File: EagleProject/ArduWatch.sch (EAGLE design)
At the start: 23 parts, among them IC1 DS1307Z, IC2 MCP73831, Q1 32.768Hz, U1 ATMEGA328P_TQFP

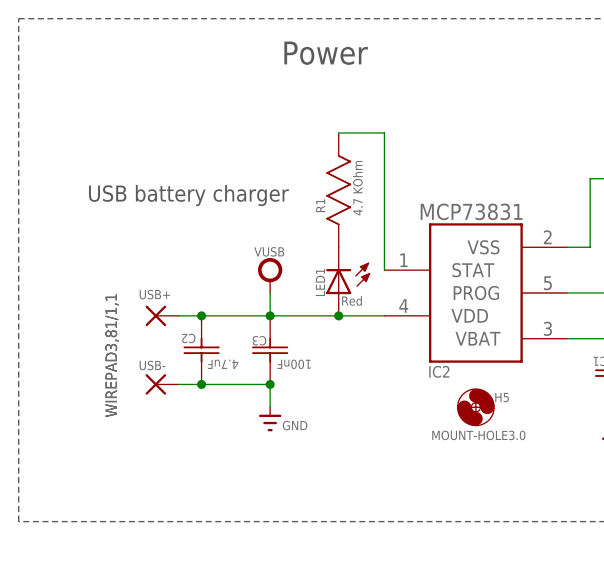
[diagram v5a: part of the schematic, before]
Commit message: USB port for charging
Implement USB port for chrging
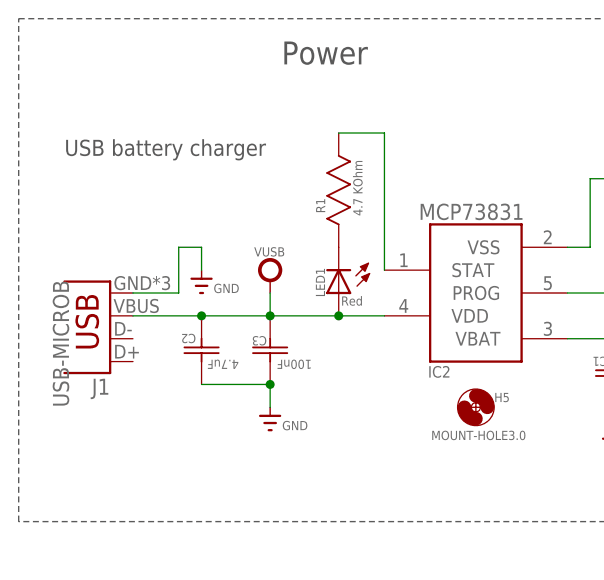
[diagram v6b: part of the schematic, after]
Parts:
- removed USB+, USB-: WIREPAD3,81/1,1, wirepad:WIREPAD3,81/1,1
- added J1: USB-MICROB, SparkFun-Connectors:USB-MICROB
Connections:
- net GND: now also J1.GND; no longer USB-.P
- net VUSB: now also J1.VBUS; no longer USB+.P
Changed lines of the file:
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@@
 <part name="Q1" library="crystal" deviceset="CRYSTAL" device="TC26H" value="32.768Hz"/>
 <part name="IC2" library="microchip-update" deviceset="MCP73831" device=""/>
-<part name="USB+" library="wirepad" deviceset="WIREPAD" device="3,81/1,1" value="WIREPAD3,81/1,1"/>
-<part name="USB-" library="wirepad" deviceset="WIREPAD" device="3,81/1,1" value="WIREPAD3,81/1,1"/>
 <part name="GND1" library="supply" deviceset="GND" device=""/>
 <part name="V1" library="supply" deviceset="VUSB" device=""/>
@@
 <part name="V8" library="supply" deviceset="VCC" device=""/>
 <part name="JP1" library="pinhead" deviceset="PINHD-2X3" device=""/>
+<part name="J1" library="SparkFun-Connectors" deviceset="USB" device="-MICROB"/>
+<part name="GND6" library="supply" deviceset="GND" device=""/>
 </parts>
 <sheets>
 <sheet>
 <plain>
-<text x="12.7" y="154.94" size="1.778" layer="97">USB battery charger</text>
+<text x="10.16" y="160.02" size="1.778" layer="97">USB battery charger</text>
 <wire x1="5.08" y1="175.26" x2="99.06" y2="175.26" width="0.1524" layer="97" style="longdash"/>
 <wire x1="99.06" y1="175.26" x2="99.06" y2="119.38" width="0.1524" layer="97" style="longdash"/>
@@
 <attribute name="VALUE" x="49.53" y="154.686" size="1.778" layer="96" rot="MR180"/>
 </instance>
-<instance part="USB+" gate="G$1" x="20.32" y="142.24" smashed="yes">
-<attribute name="NAME" x="18.415" y="144.0942" size="1.016" layer="95"/>
-<attribute name="VALUE" x="16.002" y="130.937" size="1.27" layer="96" rot="R90"/>
-</instance>
-<instance part="USB-" gate="G$1" x="20.32" y="134.62" smashed="yes">
-<attribute name="NAME" x="18.415" y="136.2202" size="1.016" layer="95"/>
-<attribute name="VALUE" x="16.002" y="130.937" size="1.27" layer="96" rot="R90"/>
-</instance>
 <instance part="GND1" gate="1" x="33.02" y="129.54" smashed="yes">
 <attribute name="VALUE" x="34.3535" y="129.54" size="1.016" layer="96"/>
@@
 </instance>
 <instance part="JP1" gate="A" x="218.44" y="43.18"/>
+<instance part="J1" gate="G$1" x="15.24" y="144.78" smashed="yes" rot="R180">
+<attribute name="NAME" x="15.24" y="135.255" size="1.778" layer="95" rot="R180"/>
+<attribute name="VALUE" x="8.89" y="132.08" size="1.778" layer="96" rot="MR90"/>
+</instance>
+<instance part="GND6" gate="1" x="25.4" y="144.78" smashed="yes">
+<attribute name="VALUE" x="26.7335" y="144.78" size="1.016" layer="96"/>
+</instance>
 </instances>
 <busses>
@@
 <net name="VUSB" class="0">
 <segment>
-<pinref part="USB+" gate="G$1" pin="P"/>
 <pinref part="LED1" gate="G$1" pin="A"/>
-<wire x1="22.86" y1="142.24" x2="25.4" y2="142.24" width="0.1524" layer="91"/>
 <pinref part="IC2" gate="G$1" pin="VDD"/>
 <wire x1="25.4" y1="142.24" x2="33.02" y2="142.24" width="0.1524" layer="91"/>
@@
 <junction x="25.4" y="142.24"/>
 <pinref part="C3" gate="A" pin="C2"/>
+<pinref part="J1" gate="G$1" pin="VBUS"/>
+<wire x1="25.4" y1="142.24" x2="17.78" y2="142.24" width="0.1524" layer="91"/>
 </segment>
 </net>
@@
 <pinref part="GND1" gate="1" pin="GND"/>
 <wire x1="33.02" y1="132.08" x2="33.02" y2="134.62" width="0.1524" layer="91"/>
-<pinref part="USB-" gate="G$1" pin="P"/>
 <wire x1="33.02" y1="134.62" x2="25.4" y2="134.62" width="0.1524" layer="91"/>
 <pinref part="C2" gate="A" pin="C1"/>
-<wire x1="25.4" y1="134.62" x2="22.86" y2="134.62" width="0.1524" layer="91"/>
-<junction x="25.4" y="134.62"/>
 <pinref part="C3" gate="A" pin="C1"/>
 <junction x="33.02" y="134.62"/>
@@
 <label x="231.14" y="40.64" size="1.016" layer="95" xref="yes"/>
 </segment>
+<segment>
+<pinref part="J1" gate="G$1" pin="GND"/>
+<wire x1="17.78" y1="144.78" x2="22.86" y2="144.78" width="0.1524" layer="91"/>
+<wire x1="22.86" y1="144.78" x2="22.86" y2="149.86" width="0.1524" layer="91"/>
+<pinref part="GND6" gate="1" pin="GND"/>
+<wire x1="22.86" y1="149.86" x2="25.4" y2="149.86" width="0.1524" layer="91"/>
+<wire x1="25.4" y1="149.86" x2="25.4" y2="147.32" width="0.1524" layer="91"/>
+</segment>
 </net>

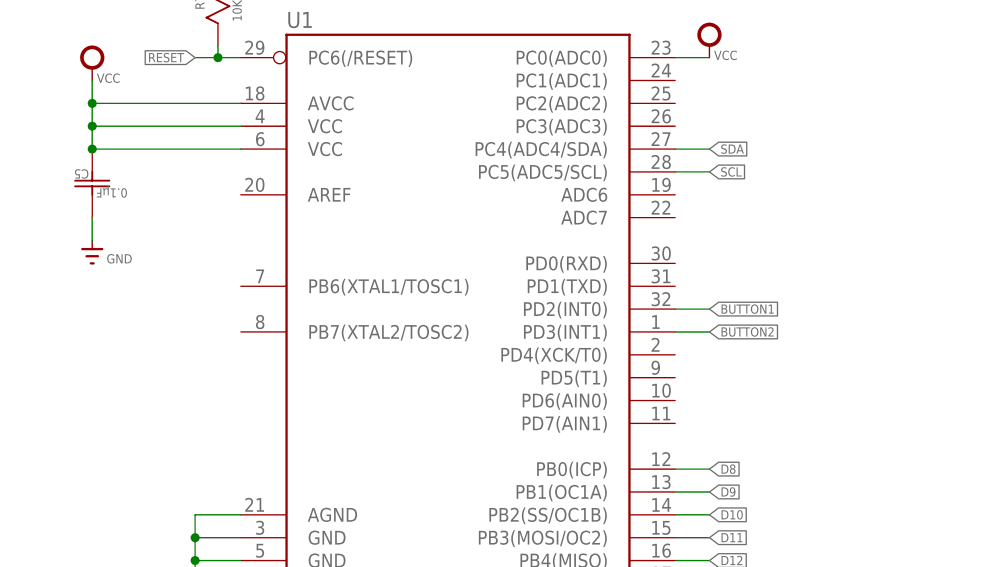
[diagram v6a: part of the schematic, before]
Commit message: Add CRYSTAL
Add CRYSTAL 8MHz
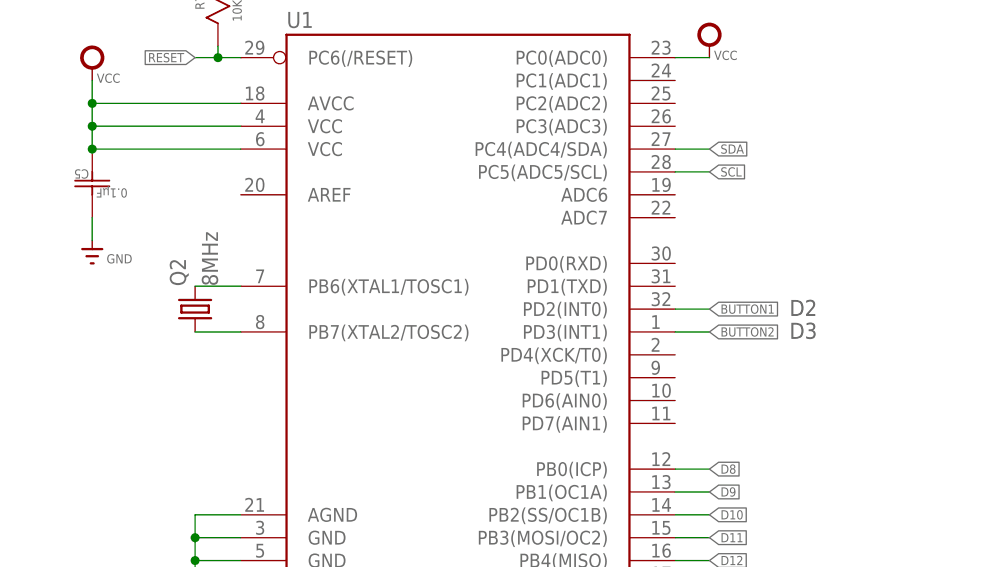
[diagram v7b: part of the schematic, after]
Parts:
- added Q2: 8MHz, crystal:CRYSTALHC49S
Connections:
- new net N$8: Q2.2, U1.PB6(XTAL1/TOSC1)
- new net N$9: Q2.1, U1.PB7(XTAL2/TOSC2)
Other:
- note added: "D2"
- note added: "D3"
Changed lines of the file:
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@@
 <part name="J1" library="SparkFun-Connectors" deviceset="USB" device="-MICROB"/>
 <part name="GND6" library="supply" deviceset="GND" device=""/>
+<part name="Q2" library="crystal" deviceset="CRYSTAL" device="HC49S" value="8MHz"/>
 </parts>
 <sheets>
@@
 <wire x1="190.5" y1="27.94" x2="190.5" y2="60.96" width="0.1524" layer="97" style="longdash"/>
 <text x="204.47" y="57.15" size="2.54" layer="97">SPI - programmer</text>
+<text x="134.62" y="64.008" size="1.778" layer="97">D2</text>
+<text x="134.62" y="61.468" size="1.778" layer="97">D3</text>
 </plain>
 <instances>
@@
 <attribute name="VALUE" x="26.7335" y="144.78" size="1.016" layer="96"/>
 </instance>
+<instance part="Q2" gate="G$1" x="68.58" y="64.77" rot="R90"/>
 </instances>
 <busses>
@@
 </segment>
 </net>
+<net name="N$8" class="0">
+<segment>
+<pinref part="U1" gate="U$1" pin="PB6(XTAL1/TOSC1)"/>
+<pinref part="Q2" gate="G$1" pin="2"/>
+<wire x1="73.66" y1="67.31" x2="68.58" y2="67.31" width="0.1524" layer="91"/>
+</segment>
+</net>
+<net name="N$9" class="0">
+<segment>
+<pinref part="U1" gate="U$1" pin="PB7(XTAL2/TOSC2)"/>
+<pinref part="Q2" gate="G$1" pin="1"/>
+<wire x1="73.66" y1="62.23" x2="68.58" y2="62.23" width="0.1524" layer="91"/>
+</segment>
+</net>
